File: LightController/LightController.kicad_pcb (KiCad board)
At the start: 2 copper layers, 140 x 55 mm, 6 parts, among them J1 Conn_01x04_Male, U1 mh-et-live-minikit, U2 TLC59208F, U3 TLC59208F, U4 TLC59208F, U5 TLC59208F

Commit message: routing almost done
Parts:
- added BTN1: SW_Push_Open, Button_Switch_SMD:SW_SPST_Omron_B3FS-101xP, F.Cu at (84.2, 47.2)
- added BTN2: SW_Push_Open, Button_Switch_SMD:SW_SPST_Omron_B3FS-101xP, F.Cu at (69.4, 47.2)
- added D1: LED, LED_SMD:LED_0603_1608Metric, F.Cu at (118.3, 44.4)
- added D2: LED, LED_SMD:LED_0603_1608Metric, F.Cu at (123.8, 51.3)
- added D3: LED, LED_SMD:LED_0603_1608Metric, F.Cu at (125.3, 51.3)
- added D4: LED, LED_SMD:LED_0603_1608Metric, F.Cu at (118.3, 48.9)
- added D5: LED, LED_SMD:LED_0603_1608Metric, F.Cu at (126.7, 51.3)
- added D6: LED, LED_SMD:LED_0603_1608Metric, F.Cu at (128.2, 51.3)
- added F1: Fuse, Fuse:Fuseholder_Cylinder-5x20mm_Schurter_0031_8201_Horizontal_Open, F.Cu at (134.9, 48.8)
- added J0: Conn_01x08_Female, bouni:SPTAF_1_8_3_5_EL, F.Cu at (37.0, 70.0)
- added J2: Conn_01x08_Female, bouni:SPTAF_1_8_3_5_EL, F.Cu at (63.5, 70.0)
- added J3: Conn_01x08_Female, bouni:SPTAF_1_8_3_5_EL, F.Cu at (76.8, 70.0)
- added J4: Conn_01x08_Female, bouni:SPTAF_1_8_3_5_EL, F.Cu at (90.0, 70.0)
- added J5: Conn_01x08_Female, bouni:SPTAF_1_8_3_5_EL, F.Cu at (103.2, 70.0)
- added J6: Conn_01x08_Female, bouni:SPTAF_1_8_3_5_EL, F.Cu at (116.5, 70.0)
- added J7: Conn_01x08_Female, bouni:SPTAF_1_8_3_5_EL, F.Cu at (129.8, 70.0)
- added J8: Conn_01x02_Female, Connector_Phoenix_MC:PhoenixContact_MC_1,5_2-G-3.5_1x02_P3.50mm_Horizontal, F.Cu at (161.5, 50.5)
- added JP1: Jumper_2_Open, Jumper:SolderJumper-2_P1.3mm_Open_RoundedPad1.0x1.5mm, F.Cu at (114.1, 46.7)
- added Q0: IRLML0030, Package_TO_SOT_SMD:SOT-23, B.Cu at (37.0, 80.8)
- added Q1: IRLML0030, Package_TO_SOT_SMD:SOT-23, B.Cu at (37.0, 73.8)
- added Q10: IRLML0030, Package_TO_SOT_SMD:SOT-23, B.Cu at (63.5, 66.8)
- added Q11: IRLML0030, Package_TO_SOT_SMD:SOT-23, B.Cu at (63.5, 59.8)
- added Q12: IRLML0030, Package_TO_SOT_SMD:SOT-23, B.Cu at (76.8, 80.8)
- added Q13: IRLML0030, Package_TO_SOT_SMD:SOT-23, B.Cu at (76.8, 73.8)
- added Q14: IRLML0030, Package_TO_SOT_SMD:SOT-23, B.Cu at (76.8, 66.8)
- added Q15: IRLML0030, Package_TO_SOT_SMD:SOT-23, B.Cu at (76.8, 59.9)
- added Q16: IRLML0030, Package_TO_SOT_SMD:SOT-23, B.Cu at (90.0, 80.8)
- added Q17: IRLML0030, Package_TO_SOT_SMD:SOT-23, B.Cu at (90.0, 73.8)
- added Q18: IRLML0030, Package_TO_SOT_SMD:SOT-23, B.Cu at (90.0, 66.8)
- added Q19: IRLML0030, Package_TO_SOT_SMD:SOT-23, B.Cu at (90.0, 59.8)
- added Q2: IRLML0030, Package_TO_SOT_SMD:SOT-23, B.Cu at (37.0, 66.8)
- added Q20: IRLML0030, Package_TO_SOT_SMD:SOT-23, B.Cu at (103.2, 80.8)
- added Q21: IRLML0030, Package_TO_SOT_SMD:SOT-23, B.Cu at (103.2, 73.8)
- added Q22: IRLML0030, Package_TO_SOT_SMD:SOT-23, B.Cu at (103.2, 66.8)
- added Q23: IRLML0030, Package_TO_SOT_SMD:SOT-23, B.Cu at (103.2, 59.7)
- added Q24: IRLML0030, Package_TO_SOT_SMD:SOT-23, B.Cu at (116.5, 80.8)
- added Q25: IRLML0030, Package_TO_SOT_SMD:SOT-23, B.Cu at (116.5, 73.8)
- added Q26: IRLML0030, Package_TO_SOT_SMD:SOT-23, B.Cu at (116.5, 66.8)
- added Q27: IRLML0030, Package_TO_SOT_SMD:SOT-23, B.Cu at (116.5, 59.8)
- added Q28: IRLML0030, Package_TO_SOT_SMD:SOT-23, B.Cu at (129.8, 80.8)
- added Q29: IRLML0030, Package_TO_SOT_SMD:SOT-23, B.Cu at (129.8, 73.8)
- added Q3: IRLML0030, Package_TO_SOT_SMD:SOT-23, B.Cu at (37.0, 59.8)
- added Q30: IRLML0030, Package_TO_SOT_SMD:SOT-23, B.Cu at (129.8, 66.8)
- added Q31: IRLML0030, Package_TO_SOT_SMD:SOT-23, B.Cu at (129.8, 59.8)
- added Q32: IRLML0030, Package_TO_SOT_SMD:SOT-23, B.Cu at (139.1, 46.7)
- added Q33: IRLML0030, Package_TO_SOT_SMD:SOT-23, B.Cu at (139.1, 50.1)
- added Q34: IRLML0030, Package_TO_SOT_SMD:SOT-23, B.Cu at (143.0, 46.7)
- added Q35: IRLML0030, Package_TO_SOT_SMD:SOT-23, B.Cu at (143.0, 50.1)
- added Q4: IRLML0030, Package_TO_SOT_SMD:SOT-23, B.Cu at (50.2, 80.8)
- added Q5: IRLML0030, Package_TO_SOT_SMD:SOT-23, B.Cu at (50.2, 73.8)
- added Q6: IRLML0030, Package_TO_SOT_SMD:SOT-23, B.Cu at (50.2, 66.8)
- added Q7: IRLML0030, Package_TO_SOT_SMD:SOT-23, B.Cu at (50.2, 59.8)
- added Q8: IRLML0030, Package_TO_SOT_SMD:SOT-23, B.Cu at (63.5, 80.8)
- added Q9: IRLML0030, Package_TO_SOT_SMD:SOT-23, B.Cu at (63.5, 73.8)
- added R1: 10K, Resistor_SMD:R_0603_1608Metric, B.Cu at (114.1, 46.7)
- added R2: R, Resistor_SMD:R_0603_1608Metric, B.Cu at (118.3, 44.4)
- added R3: R, Resistor_SMD:R_0603_1608Metric, B.Cu at (123.8, 51.3)
- added R4: R, Resistor_SMD:R_0603_1608Metric, B.Cu at (125.3, 51.3)
- added R5: R, Resistor_SMD:R_0603_1608Metric, B.Cu at (118.3, 47.4)
- added R6: R, Resistor_SMD:R_0603_1608Metric, B.Cu at (126.7, 51.3)
- added R7: R, Resistor_SMD:R_0603_1608Metric, B.Cu at (128.2, 51.3)
- added RN1: 10k, Resistor_SMD:R_Array_Concave_4x0603, B.Cu at (43.6, 82.2)
- added RN2: 10k, Resistor_SMD:R_Array_Concave_4x0603, B.Cu at (56.9, 82.2)
- added RN3: 10k, Resistor_SMD:R_Array_Concave_4x0603, B.Cu at (70.1, 82.2)
- added RN4: 10k, Resistor_SMD:R_Array_Concave_4x0603, B.Cu at (83.3, 82.2)
- added RN5: 10k, Resistor_SMD:R_Array_Concave_4x0603, B.Cu at (96.6, 82.2)
- added RN6: 10k, Resistor_SMD:R_Array_Concave_4x0603, B.Cu at (109.9, 82.2)
- added RN7: 10k, Resistor_SMD:R_Array_Concave_4x0603, B.Cu at (123.1, 82.2)
- added RN8: 10k, Resistor_SMD:R_Array_Concave_4x0603, B.Cu at (136.4, 82.2)
- added RN9: 10k, Resistor_SMD:R_Array_Concave_4x0603, B.Cu at (140.3, 53.5)
- J1: value Conn_01x04_Male -> Conn_01x08_Female; footprint Connector_Phoenix_MC:PhoenixContact_MCV_1,5_4-G-3.5_1x04_P3.50mm_Vertical -> bouni:SPTAF_1_8_3_5_EL
- U2, U3: value TLC59208F -> MCP23017_SO; footprint Package_SO:TSSOP-16_4.4x5mm_P0.65mm -> Package_SO:SSOP-28_5.3x10.2mm_P0.65mm; moved to B.Cu
- U4: value TLC59208F -> D-SUN-MP1584EN; footprint Package_SO:TSSOP-16_4.4x5mm_P0.65mm -> bouni:D-SUN-MP1584EN
- U5: value TLC59208F -> DHT22; footprint Package_SO:TSSOP-16_4.4x5mm_P0.65mm -> Sensor:Aosong_DHT11_5.5x12.0_P2.54mm
- moved U4 71.5 mm to (148.9, 69.9)
- moved U5 53.4 mm to (130.4, 46.7), turned to -90 degrees
- moved U3 40.3 mm to (106.6, 48.3), turned to 90 degrees
- moved J1 30.9 mm to (50.2, 70.0), turned to 90 degrees
- moved U1 17.2 mm to (155.0, 69.8), turned to 90 degrees
- moved U2 17.2 mm to (53.6, 48.3), turned to 90 degrees
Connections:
- J1 pad 1: unconnected-(J1-Pad1) -> +12V
- J1 pad 2: unconnected-(J1-Pad2) -> OUT4
- J1 pad 3: unconnected-(J1-Pad3) -> +12V
- J1 pad 4: unconnected-(J1-Pad4) -> OUT5
- U1 pad 11: unconnected-(U1-Pad11) -> Net-(JP1-Pad2)
- U1 pad 18: unconnected-(U1-Pad18) -> +3V3
- U1 pad 25: unconnected-(U1-Pad25) -> BTN1
- U1 pad 26: unconnected-(U1-Pad26) -> BTN2
- U1 pad 28: 5V -> +5V
- U1 pad 32: unconnected-(U1-Pad32) -> DHT22
- U1 pad 33: unconnected-(U1-Pad33) -> LED1
- U1 pad 34: unconnected-(U1-Pad34) -> LED2
- U1 pad 35: unconnected-(U1-Pad35) -> LED3
- U1 pad 36: unconnected-(U1-Pad36) -> LED4
- U2 pad 1: unconnected-(U2-Pad1) -> GPIO8
- U2 pad 10: unconnected-(U2-Pad10) -> +5V
- U2 pad 12: unconnected-(U2-Pad12) -> SCL
- U2 pad 13: unconnected-(U2-Pad13) -> SDA
- U2 pad 14: SCL -> unconnected-(U2-Pad14)
- U2 pad 15: SDA -> GND
- U2 pad 16: +5V -> GND
- U2 pad 2: unconnected-(U2-Pad2) -> GPIO9
- U2 pad 3: unconnected-(U2-Pad3) -> GPIO10
- U2 pad 4: unconnected-(U2-Pad4) -> GPIO11
- U2 pad 5: unconnected-(U2-Pad5) -> GPIO12
- U2 pad 6: unconnected-(U2-Pad6) -> GPIO13
- U2 pad 7: unconnected-(U2-Pad7) -> GPIO14
- U2 pad 8: GND -> GPIO15
- U2 pad 9: unconnected-(U2-Pad9) -> GND
- U3 pad 1: unconnected-(U3-Pad1) -> GPIO24
- U3 pad 10: unconnected-(U3-Pad10) -> +5V
- U3 pad 12: unconnected-(U3-Pad12) -> SCL
- U3 pad 13: unconnected-(U3-Pad13) -> SDA
- U3 pad 14: SCL -> unconnected-(U3-Pad14)
- U3 pad 15: SDA -> +5V
- U3 pad 16: +5V -> GND
- U3 pad 2: unconnected-(U3-Pad2) -> GPIO25
- U3 pad 3: unconnected-(U3-Pad3) -> GPIO26
- U3 pad 4: unconnected-(U3-Pad4) -> GPIO27
- U3 pad 5: unconnected-(U3-Pad5) -> GPIO28
- U3 pad 6: unconnected-(U3-Pad6) -> GPIO29
- U3 pad 7: unconnected-(U3-Pad7) -> GPIO30
- U3 pad 8: GND -> GPIO31
- U3 pad 9: unconnected-(U3-Pad9) -> GND
- U4 pad 1: unconnected-(U4-Pad1) -> GND
- U4 pad 2: unconnected-(U4-Pad2) -> GND
- U4 pad 3: unconnected-(U4-Pad3) -> +12V
- U4 pad 4: unconnected-(U4-Pad4) -> +12V
- U4 pad 5: unconnected-(U4-Pad5) -> GND
- U4 pad 6: unconnected-(U4-Pad6) -> GND
- U4 pad 7: unconnected-(U4-Pad7) -> +5V
- U4 pad 8: GND -> +5V
- U5 pad 1: unconnected-(U5-Pad1) -> +3V3
- U5 pad 2: unconnected-(U5-Pad2) -> DHT22
- U5 pad 4: unconnected-(U5-Pad4) -> GND
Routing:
- net +12V: track 0.00 -> 299.5 mm, vias 0 -> 1
- net +5V: track 0.00 -> 175.0 mm, vias 0 -> 6
- net BTN2: track 0.00 -> 118.3 mm, vias 0 -> 4
- net SDA: track 0.00 -> 111.8 mm, vias 0 -> 5
- net SCL: track 0.00 -> 107.1 mm, vias 0 -> 5
- net BTN1: track 0.00 -> 101.1 mm, vias 0 -> 4
- net +3V3: track 0.00 -> 78.8 mm
- net GPIO15: track 0.00 -> 74.7 mm, vias 0 -> 2
- net GPIO14: track 0.00 -> 72.2 mm, vias 0 -> 2
- net GPIO13: track 0.00 -> 69.7 mm, vias 0 -> 2
- net GPIO31: track 0.00 -> 69.1 mm, vias 0 -> 2
- net RESET: track 0.00 -> 68.6 mm, vias 0 -> 3
- net GPIO12: track 0.00 -> 67.3 mm, vias 0 -> 2
- net GPIO30: track 0.00 -> 65.5 mm, vias 0 -> 2
- net GPIO29: track 0.00 -> 63.2 mm, vias 0 -> 2
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- added copper zone on B.Cu, net +12V
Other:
- board size 140 x 55 mm -> 140 x 42 mm

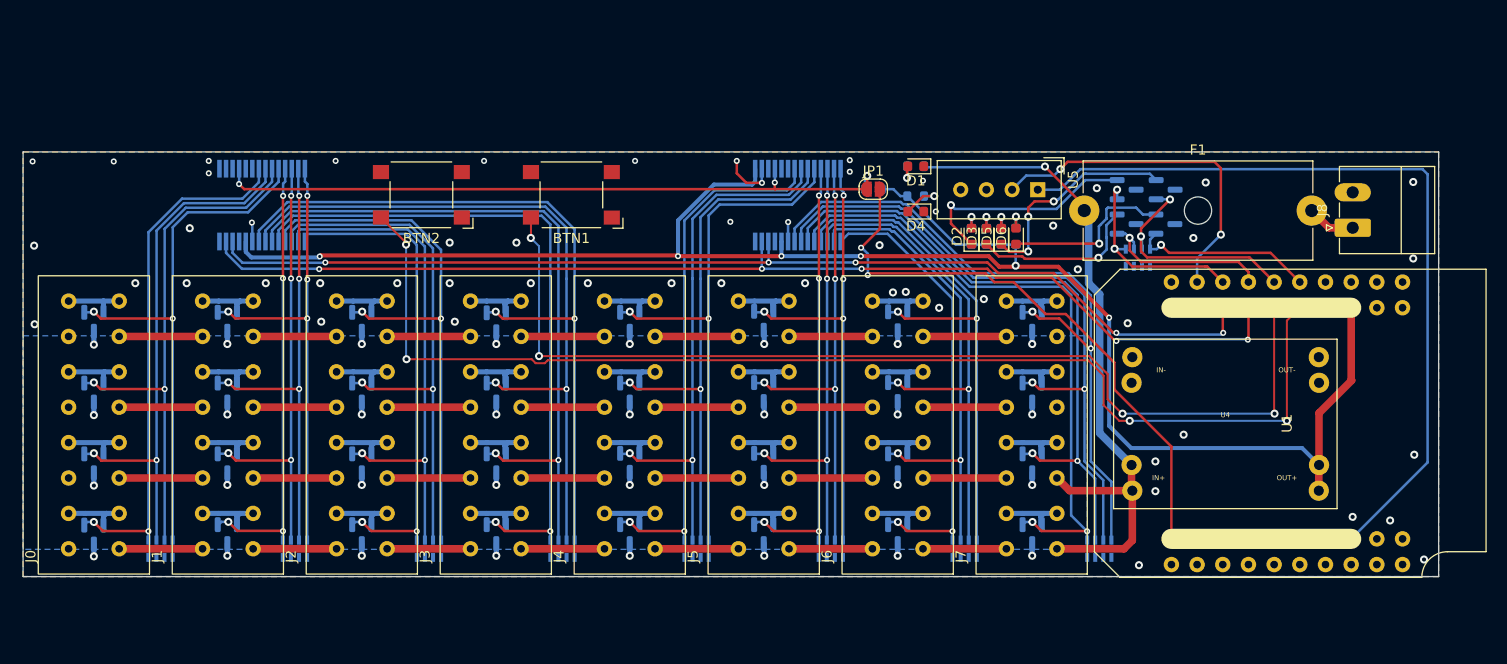
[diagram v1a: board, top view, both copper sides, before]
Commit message: made pcb slightly bigger for mounting holes
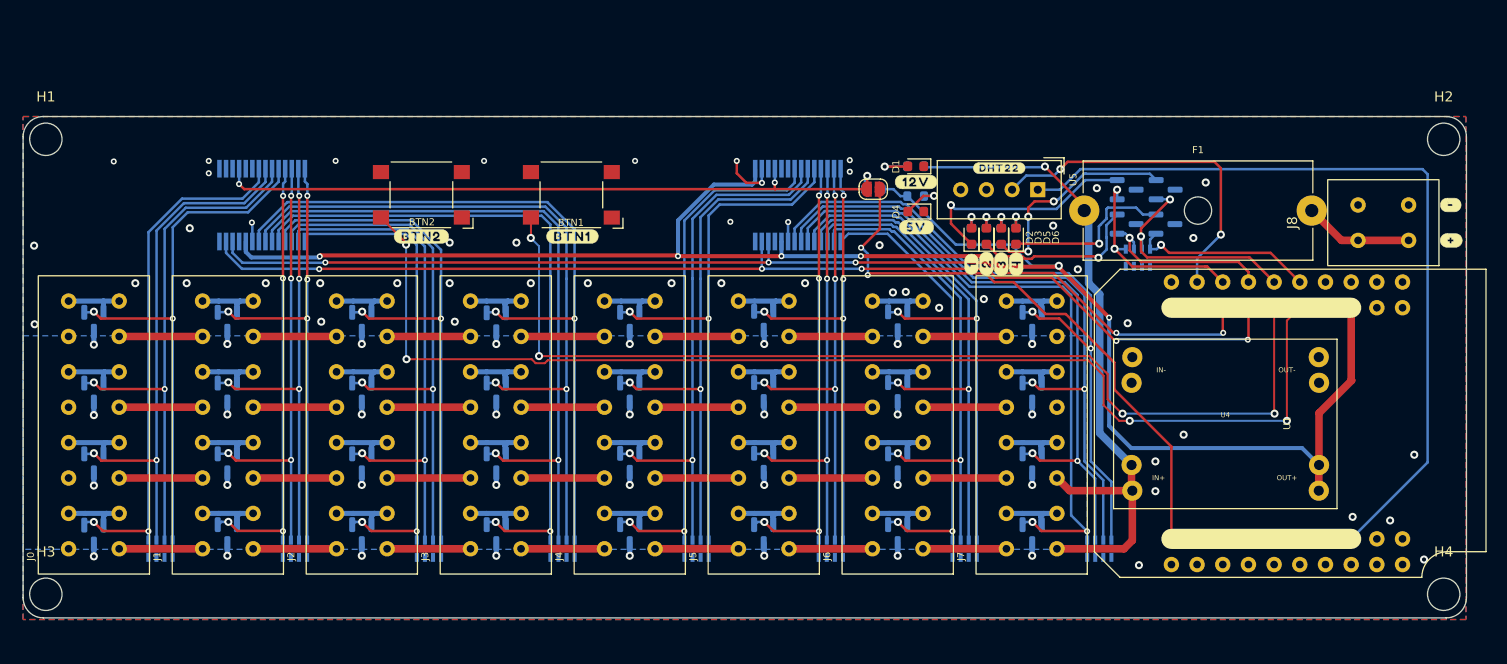
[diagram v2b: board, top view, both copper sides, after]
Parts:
- added ?: , buzzardLabel, F.Cu at (84.3, 51.4)
- added ?: , buzzardLabel, F.Cu at (126.7, 54.1)
- added ?: , buzzardLabel, F.Cu at (123.8, 54.1)
- added ?: , buzzardLabel, F.Cu at (118.3, 46.0)
- added ?: , buzzardLabel, F.Cu at (69.4, 51.4)
- added ?: , buzzardLabel, F.Cu at (125.3, 54.1)
- added ?: , buzzardLabel, F.Cu at (126.5, 44.6)
- added ?: , buzzardLabel, F.Cu at (171.2, 48.2)
- added ?: , buzzardLabel, F.Cu at (171.2, 51.8)
- added ?: , buzzardLabel, F.Cu at (128.2, 54.1)
- added ?: , buzzardLabel, F.Cu at (118.4, 50.4)
- added H1: MountingHole, MountingHole:MountingHole_3.2mm_M3, F.Cu at (32.2, 41.8)
- added H2: MountingHole, MountingHole:MountingHole_3.2mm_M3, F.Cu at (170.5, 41.8)
- added H3: MountingHole, MountingHole:MountingHole_3.2mm_M3, F.Cu at (32.2, 86.8)
- added H4: MountingHole, MountingHole:MountingHole_3.2mm_M3, F.Cu at (170.5, 86.8)
- J8: footprint Connector_Phoenix_MC:PhoenixContact_MC_1,5_2-G-3.5_1x02_P3.50mm_Horizontal -> bouni:SPTAF_1_2_3_5_EL
- moved J8 3.07 mm to (164.5, 50.0)
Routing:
- net Net-(F1-Pad2): track 4.75 -> 10.8 mm
- net +5V: track 175.0 -> 178.3 mm
- net Net-(D1-Pad2): track 2.32 -> 4.53 mm
- net GND: vias 87 -> 82
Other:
- board size 140 x 42 mm -> 142.8 x 49.6 mm

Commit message: started positioning labels
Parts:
- added H5: MountingHole, MountingHole:MountingHole_3.2mm_M3, F.Cu at (96.5, 89.2)
- added H6: MountingHole, MountingHole:MountingHole_3.2mm_M3, F.Cu at (96.5, 41.8)
- JP1: moved to B.Cu
- moved ? 33.0 mm to (158.5, 41.0), turned to 0 degrees
- moved ? 31.6 mm to (155.5, 41.0), turned to 0 degrees
- moved D6 31.5 mm to (158.5, 42.8), turned to 180 degrees
- moved R7 31.5 mm to (158.5, 42.8), turned to 0 degrees
- moved ? 30.2 mm to (152.5, 41.0), turned to 0 degrees
- moved D5 30.0 mm to (155.5, 42.8), turned to 180 degrees
- moved R6 30.0 mm to (155.5, 42.8), turned to 0 degrees
- moved ? 28.8 mm to (149.5, 41.0), turned to 0 degrees
- moved D3 28.6 mm to (152.5, 42.8), turned to 180 degrees
- moved R4 28.6 mm to (152.5, 42.8), turned to 0 degrees
- moved R5 27.3 mm to (145.2, 42.8), turned to 0 degrees
- moved R3 27.1 mm to (149.5, 42.8), turned to 0 degrees
- moved D2 27.1 mm to (149.5, 42.8), turned to 180 degrees
- moved ? 24.0 mm to (141.8, 41.1)
- moved D1 23.6 mm to (141.8, 42.7)
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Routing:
- net +5V: track 178.3 -> 215.5 mm
- net Net-(JP1-Pad2): track 57.5 -> 36.3 mm, vias 2 -> 0
- net Net-(D2-Pad1): track 22.5 -> 2.76 mm
- net Net-(D5-Pad1): track 21.6 -> 2.72 mm, vias 3 -> 1
- net RESET: track 68.6 -> 86.1 mm
- net Net-(D3-Pad1): track 16.9 -> 2.76 mm
- net Net-(D6-Pad1): track 17.3 -> 3.86 mm
- net +12V: track 299.5 -> 286.3 mm, vias 1 -> 0
- net LED4: track 18.3 -> 31.1 mm, vias 1 -> 2
- net DHT22: track 34.3 -> 22.7 mm, vias 2 -> 0
- net Net-(D4-Pad2): track 4.23 -> 10.9 mm
- net +3V3: track 78.8 -> 84.7 mm
- net LED2: track 17.6 -> 21.6 mm, vias 1 -> 2
- net Net-(D6-Pad2): track 2.25 -> 0.00 mm, vias 1 -> 0
- net Net-(D5-Pad2): track 2.21 -> 0.00 mm, vias 1 -> 0
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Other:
- board size 142.8 x 49.6 mm -> 142.8 x 52.1 mm
